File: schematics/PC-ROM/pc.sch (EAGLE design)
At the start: 8 parts

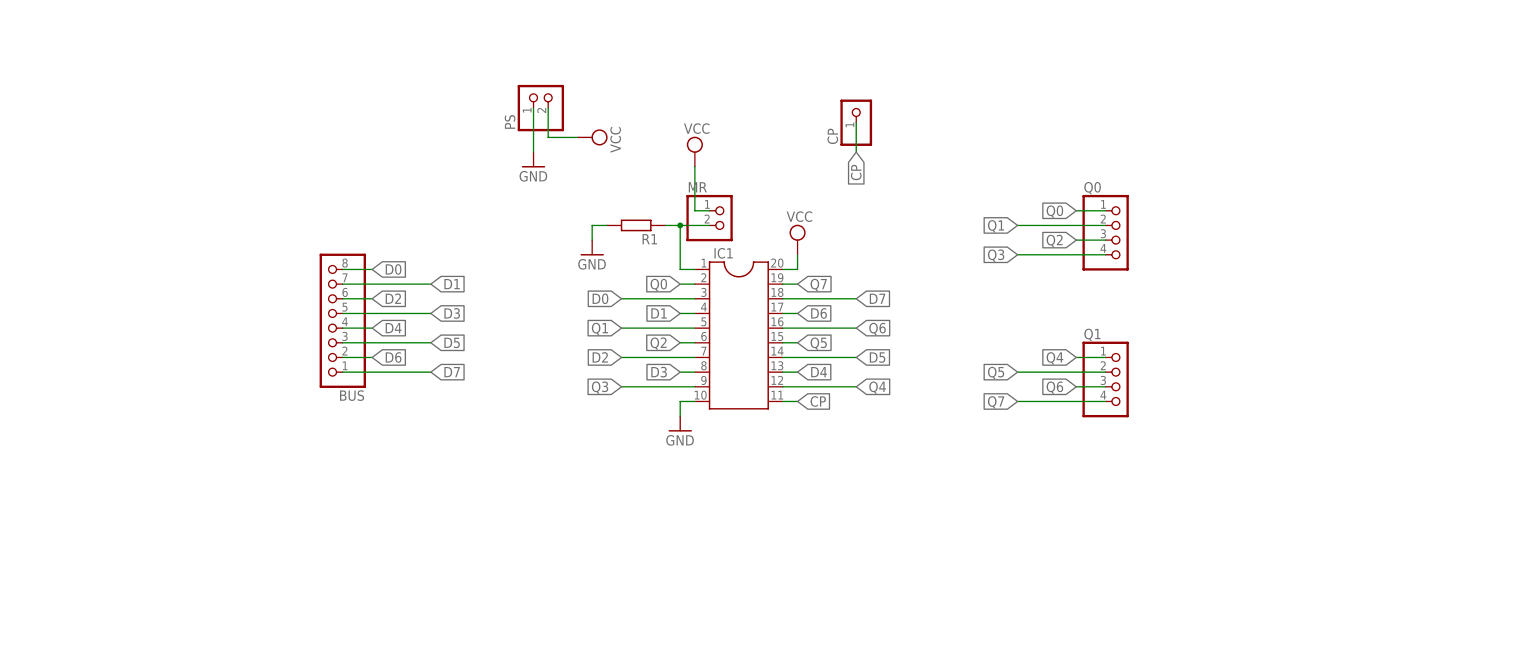
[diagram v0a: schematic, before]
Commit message: Added sch, brd and gerber file for register, register bus, pc and ROM.
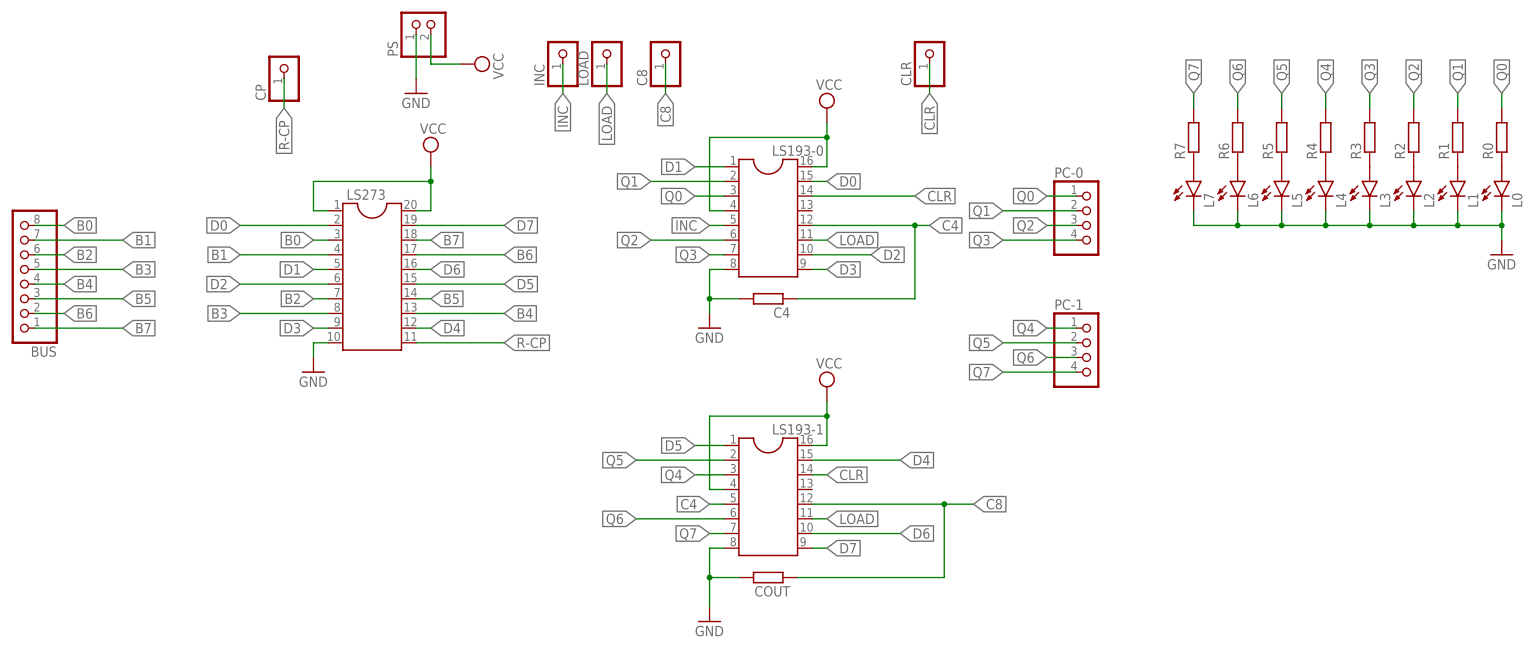
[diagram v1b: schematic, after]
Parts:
- removed IC1: (no value), ic-package:DIL20S
- removed MR: (no value), pinhead:PINHD-1X2
- removed Q0, Q1: (no value), pinhead:PINHD-1X4
- added C4, COUT, R0, R2, R3, R4, R5, R6, R7: (no value), rcl:R-EU_0204/7
- added C8, CLR, INC, LOAD: (no value), pinhead:PINHD-1X1
- added L0, L1, L2, L3, L4, L5, L6, L7: (no value), led:LED5MM
- added LS193-0, LS193-1: (no value), ic-package:DIL16S
- added LS273: (no value), ic-package:DIL20S
- added PC-0, PC-1: (no value), pinhead:PINHD-1X4
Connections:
- removed net CP: CP.1, IC1.11
- new net B0: BUS.8, LS273.3
- new net B1: BUS.7, LS273.4
- new net B2: BUS.6, LS273.7
- new net B3: BUS.5, LS273.8
- new net B4: BUS.4, LS273.13
- new net B5: BUS.3, LS273.14
- new net B6: BUS.2, LS273.17
- new net B7: BUS.1, LS273.18
- new net C4: C4.1, LS193-0.12, LS193-1.5
- new net C8: C8.1, COUT.1, LS193-1.12
- new net INC: INC.1, LS193-0.5
- new net LOAD: LOAD.1, LS193-0.11, LS193-1.11
- new net N$1: L3.A, R3.1
- new net N$2: L2.A, R2.1
- new net N$3: L1.A, R1.1
- new net N$4: L0.A, R0.1
- new net N$5: L4.A, R4.1
- new net N$6: L5.A, R5.1
- new net N$7: L6.A, R6.1
- new net N$8: L7.A, R7.1
- new net R-CP: CP.1, LS273.11
- net CLR: now also CLR.1, LS193-0.14, LS193-1.14; no longer IC1.1, MR.2, R1.1
- net D0: now also LS193-0.15, LS273.2; no longer BUS.8, IC1.3
- net D1: now also LS193-0.1, LS273.5; no longer BUS.7, IC1.4
- net D2: now also LS193-0.10, LS273.6; no longer BUS.6, IC1.7
- net D3: now also LS193-0.9, LS273.9; no longer BUS.5, IC1.8
- net D4: now also LS193-1.15, LS273.12; no longer BUS.4, IC1.13
- net D5: now also LS193-1.1, LS273.15; no longer BUS.3, IC1.14
- net D6: now also LS193-1.10, LS273.16; no longer BUS.2, IC1.17
- net D7: now also LS193-1.9, LS273.19; no longer BUS.1, IC1.18
- net GND: now also C4.2, COUT.2, L0.C, L1.C, L2.C, L3.C, L4.C, L5.C, L6.C, L7.C, LS193-0.8, LS193-1.8, LS273.10; no longer IC1.10, R1.2
- net Q0: now also LS193-0.3, PC-0.1, R0.2; no longer IC1.2, Q0.1
- net Q1: now also LS193-0.2, PC-0.2, R1.2; no longer IC1.5, Q0.2
- net Q2: now also LS193-0.6, PC-0.3, R2.2; no longer IC1.6, Q0.3
- net Q3: now also LS193-0.7, PC-0.4, R3.2; no longer IC1.9, Q0.4
- net Q4: now also LS193-1.3, PC-1.1, R4.2; no longer IC1.12, Q1.1
- net Q5: now also LS193-1.2, PC-1.2, R5.2; no longer IC1.15, Q1.2
- net Q6: now also LS193-1.6, PC-1.3, R6.2; no longer IC1.16, Q1.3
- net Q7: now also LS193-1.7, PC-1.4, R7.2; no longer IC1.19, Q1.4
- net VCC: now also LS193-0.16, LS193-0.4, LS193-1.16, LS193-1.4, LS273.1, LS273.20; no longer IC1.20, MR.1
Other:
- moved on the sheet: BUS, CP, PS, R1
